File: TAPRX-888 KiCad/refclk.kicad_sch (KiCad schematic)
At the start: 53 parts, among them J10 U.FL-R, Q1 PMOS Si2343DS, Q2 MMBT3904, U14 LP5907MFX-3.3, U16 TLV3501, U18 NC7SV157, U19 74LVC2G14, U20 Si5351A, U21 NC7SV157, U22 SN65LVDS1, X1 TCXO-27M

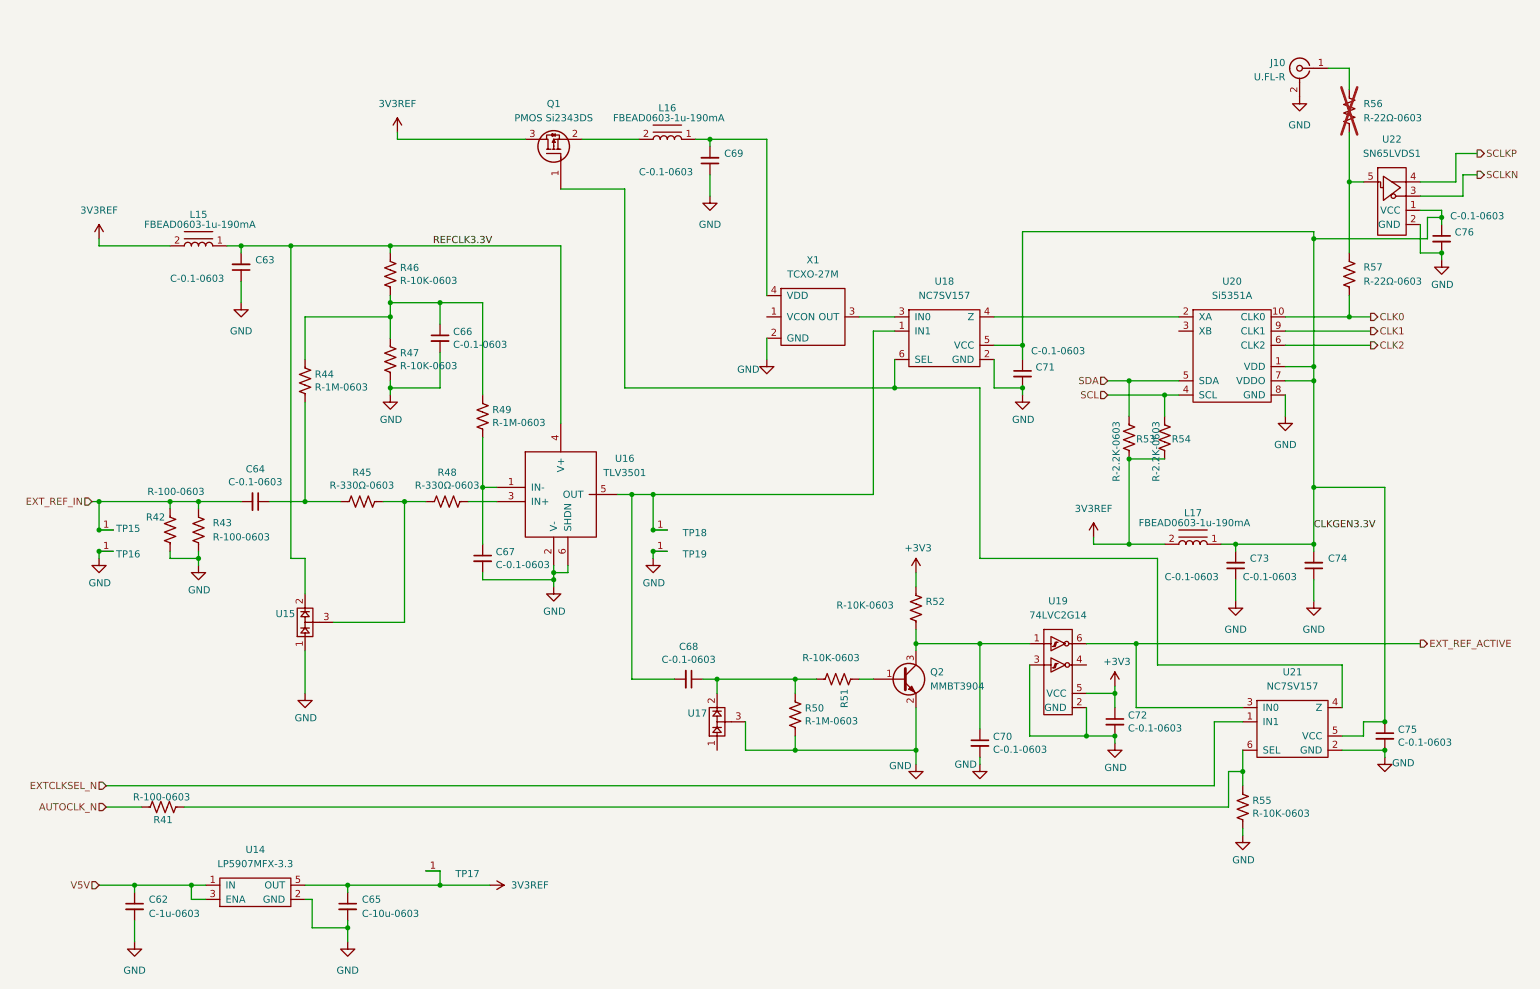
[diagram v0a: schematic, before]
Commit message: acquire Pauls' latest work
in zip file 0.3a.zip.  took its files and put into TAPRX-888 KiCad, renaming them.
Moved old work to a new folder, WB6CXC previous work.
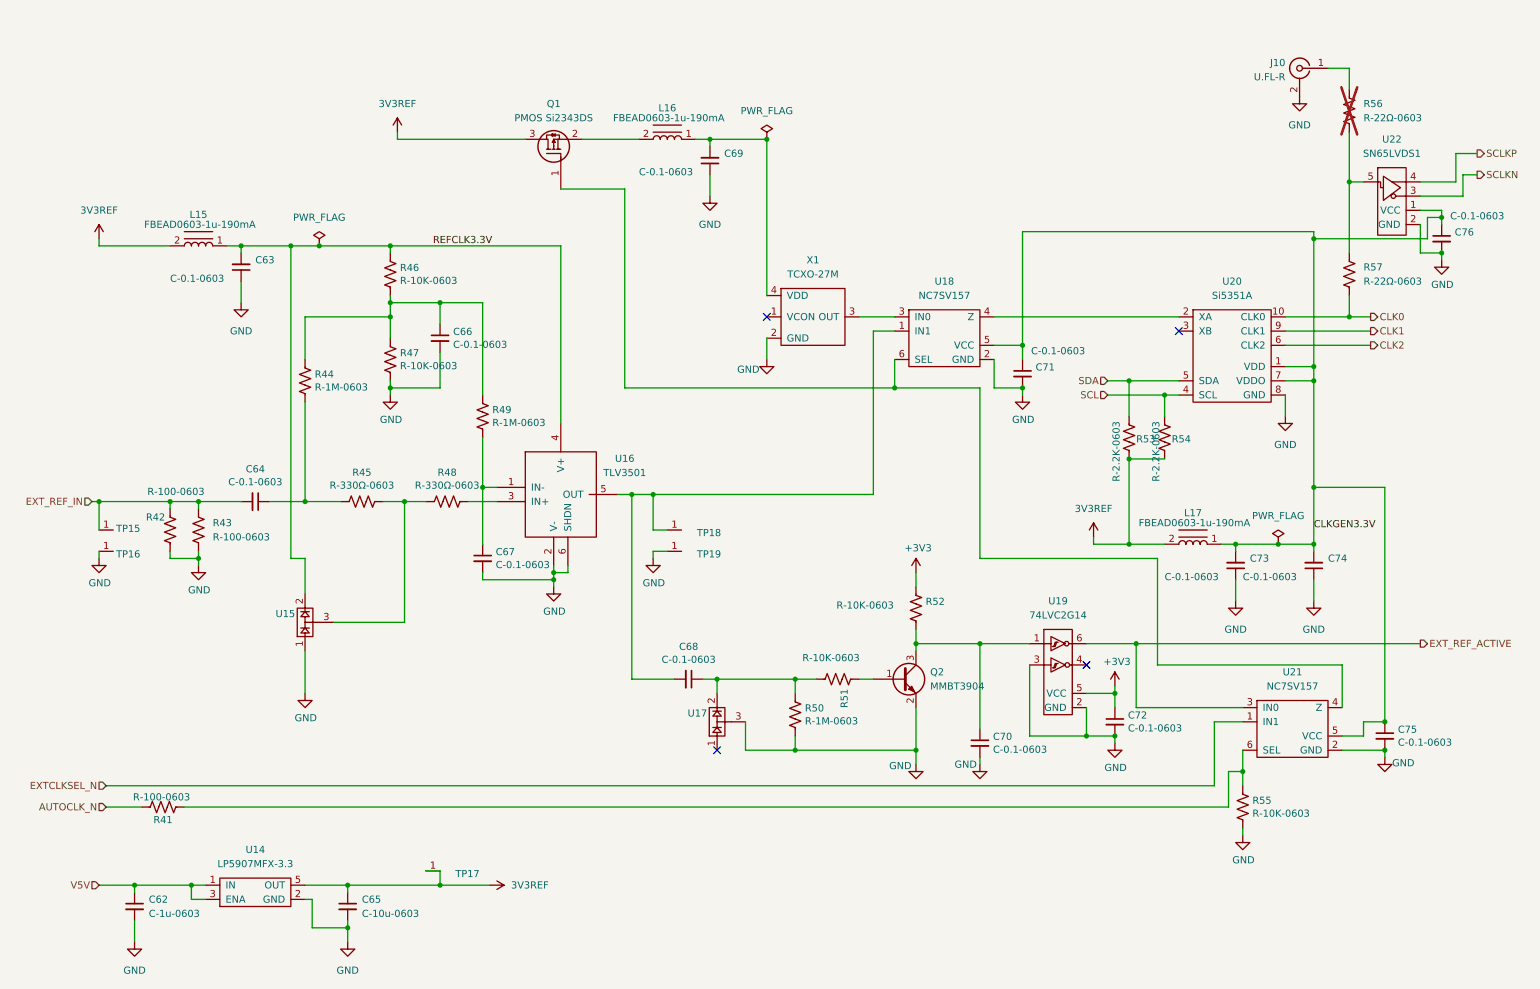
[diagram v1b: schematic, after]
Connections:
- no-connect marks 0 -> 4
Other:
- moved on the sheet: TP18, TP19

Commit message: reorg to put into main directory
moved paul's v0.4 work into the main folder
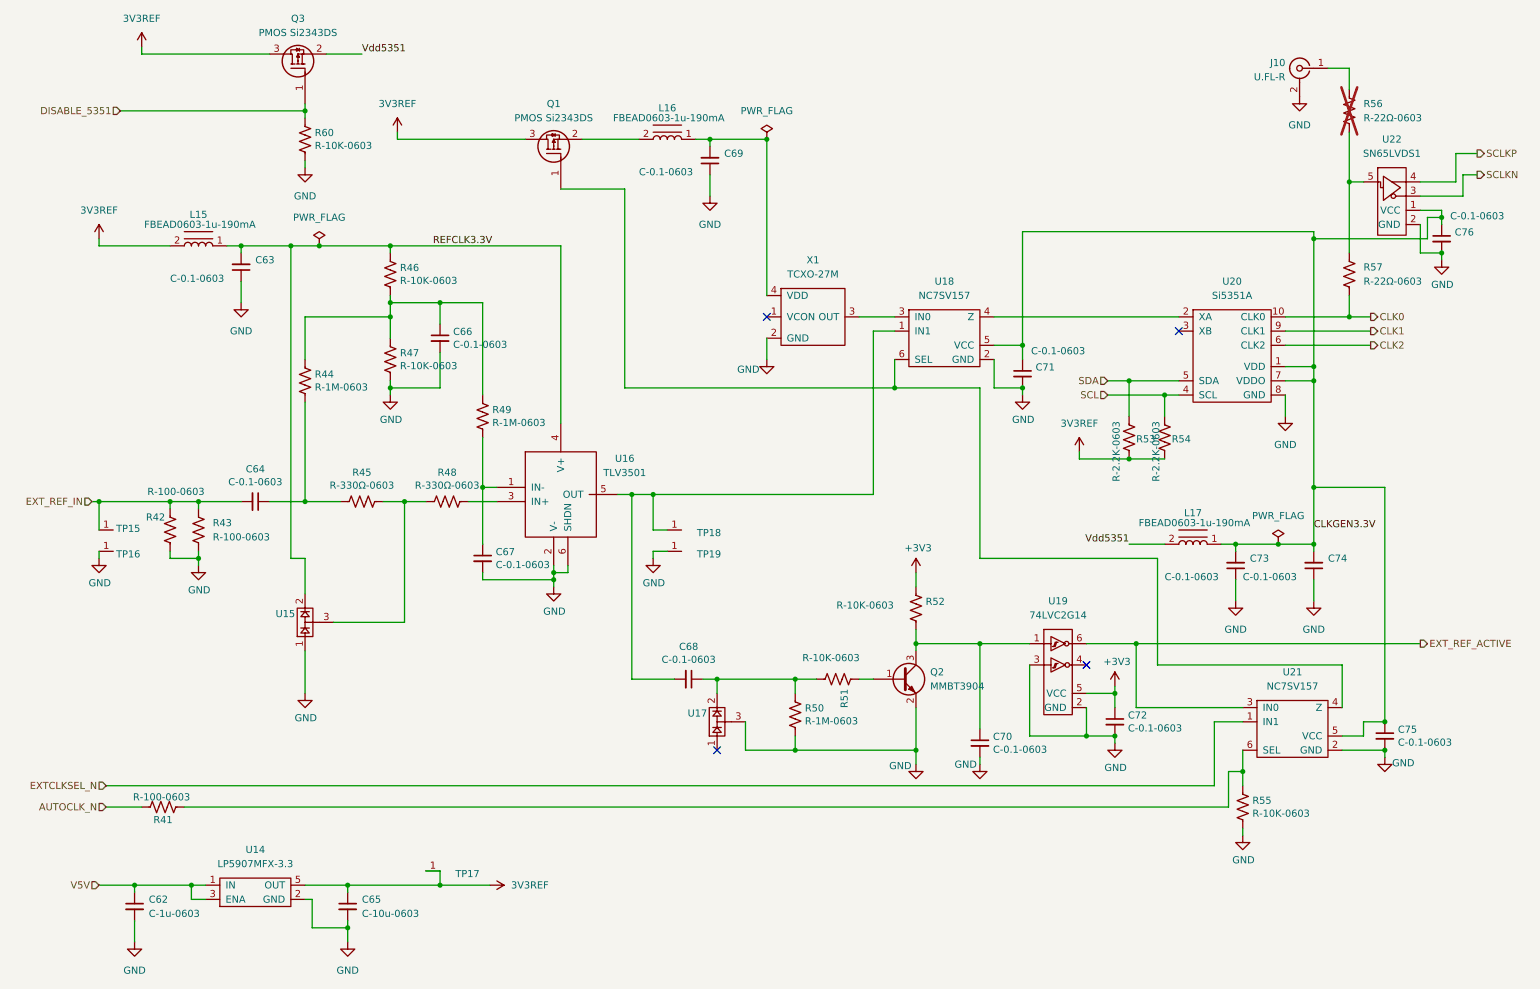
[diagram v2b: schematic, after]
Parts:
- added Q3: PMOS Si2343DS, TIS_Footprints:SOT-23, symbol TIS:PMOS Si2343DS
- added R60: R-10K-0603, TIS_Footprints:PAD_0603, symbol resistors:R-10K-0603
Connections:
- net 3V3REF: now also Q3.3 (D); no longer L17.2
- net GND: now also R60.2
- new net DISABLE_5351: Q3.1 (G), R60.1
- new net Vdd5351: L17.2, Q3.2 (S)

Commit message: Adding local KiCad symbol and footprint libraries to project
Adding local KiCad symbol and footprint libraries to project
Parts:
- C62: symbol capacitors:C-1u-0603 -> Library:C-1u-0603
- C63, C64, C66, C67, C68, C69, C70, C71, C72, C73, C74, C75, C76: symbol capacitors:C-0.1-0603 -> Library:C-0.1-0603
- C65: symbol capacitors:C-10u-0603 -> Library:C-10u-0603
- J10: symbol TIS:U.FL-R -> Library:U.FL-R
- L15, L16, L17: symbol TIS:FBEAD0603-1u-190mA -> Library:FBEAD0603-1u-190mA
- Q1, Q3: symbol TIS:PMOS Si2343DS -> Library:PMOS Si2343DS
- Q2: symbol TIS:MMBT3904 -> Library:MMBT3904
- R41, R42, R43: symbol resistors:R-100-0603 -> Library:R-100-0603
- R44, R49, R50: symbol resistors:R-1M-0603 -> Library:R-1M-0603
- R45, R48: symbol resistors:R-330Ω-0603 -> Library:R-330Ω-0603
- R46, R47, R51, R52, R55, R60: symbol resistors:R-10K-0603 -> Library:R-10K-0603
- R53, R54: symbol resistors:R-2.2K-0603 -> Library:R-2.2K-0603
- R56, R57: symbol resistors:R-22Ω-0603 -> Library:R-22Ω-0603
- TP15, TP16, TP17, TP18, TP19: symbol TIS:TP -> Library:TP
- U14: symbol TIS:LP5907MFX-3.3 -> Library:LP5907MFX-3.3
- U15, U17: symbol TIS:BAV99-Dual_Diode -> Library:BAV99-Dual_Diode
- U16: symbol TIS:TLV3501 -> Library:TLV3501
- U18, U21: symbol TIS:NC7SZ157 -> Library:NC7SZ157
- U19: symbol TIS:74LVC2G14-SC70 -> Library:74LVC2G14-SC70
- U20: symbol TIS:Si5351A -> Library:Si5351A
- U22: symbol TIS:SN65LVDS1-DIFF-DRIVER -> Library:SN65LVDS1-DIFF-DRIVER
- X1: symbol TIS:TCXO-27M-3225 -> Library:TCXO-27M-3225

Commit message: Updated ADC component data, fixed KiCad v10 zone issue
ADC name and LCSC # updated
KiCad v10 DRC changes - zone overlap and priority check failed (board OK, just DRC issue).  Fixed DRC by merging zones.
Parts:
- U15, U17: value ~ -> (none)
